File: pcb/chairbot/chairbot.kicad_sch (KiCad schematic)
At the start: 16 parts, among them J1 Conn_01x02, J2 Conn_01x05, J6 GND, U1 ESP32mini, U3 74HCT244, U4 buck-converter, U9 PCA9515

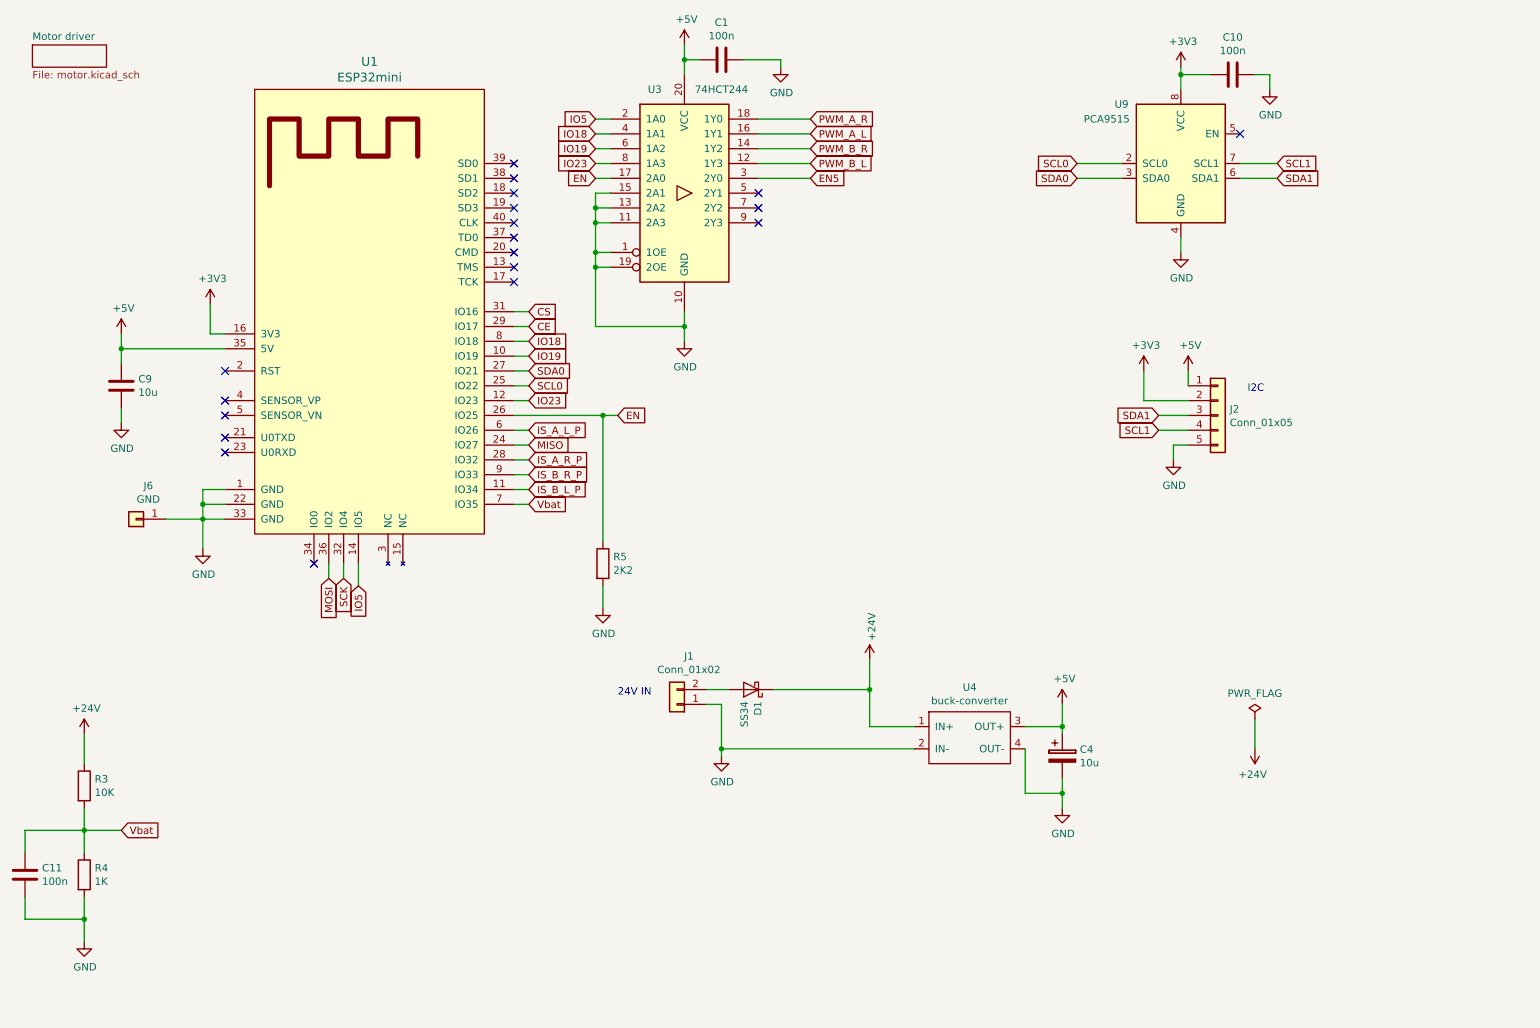
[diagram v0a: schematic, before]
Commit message: Complete overall schematic.
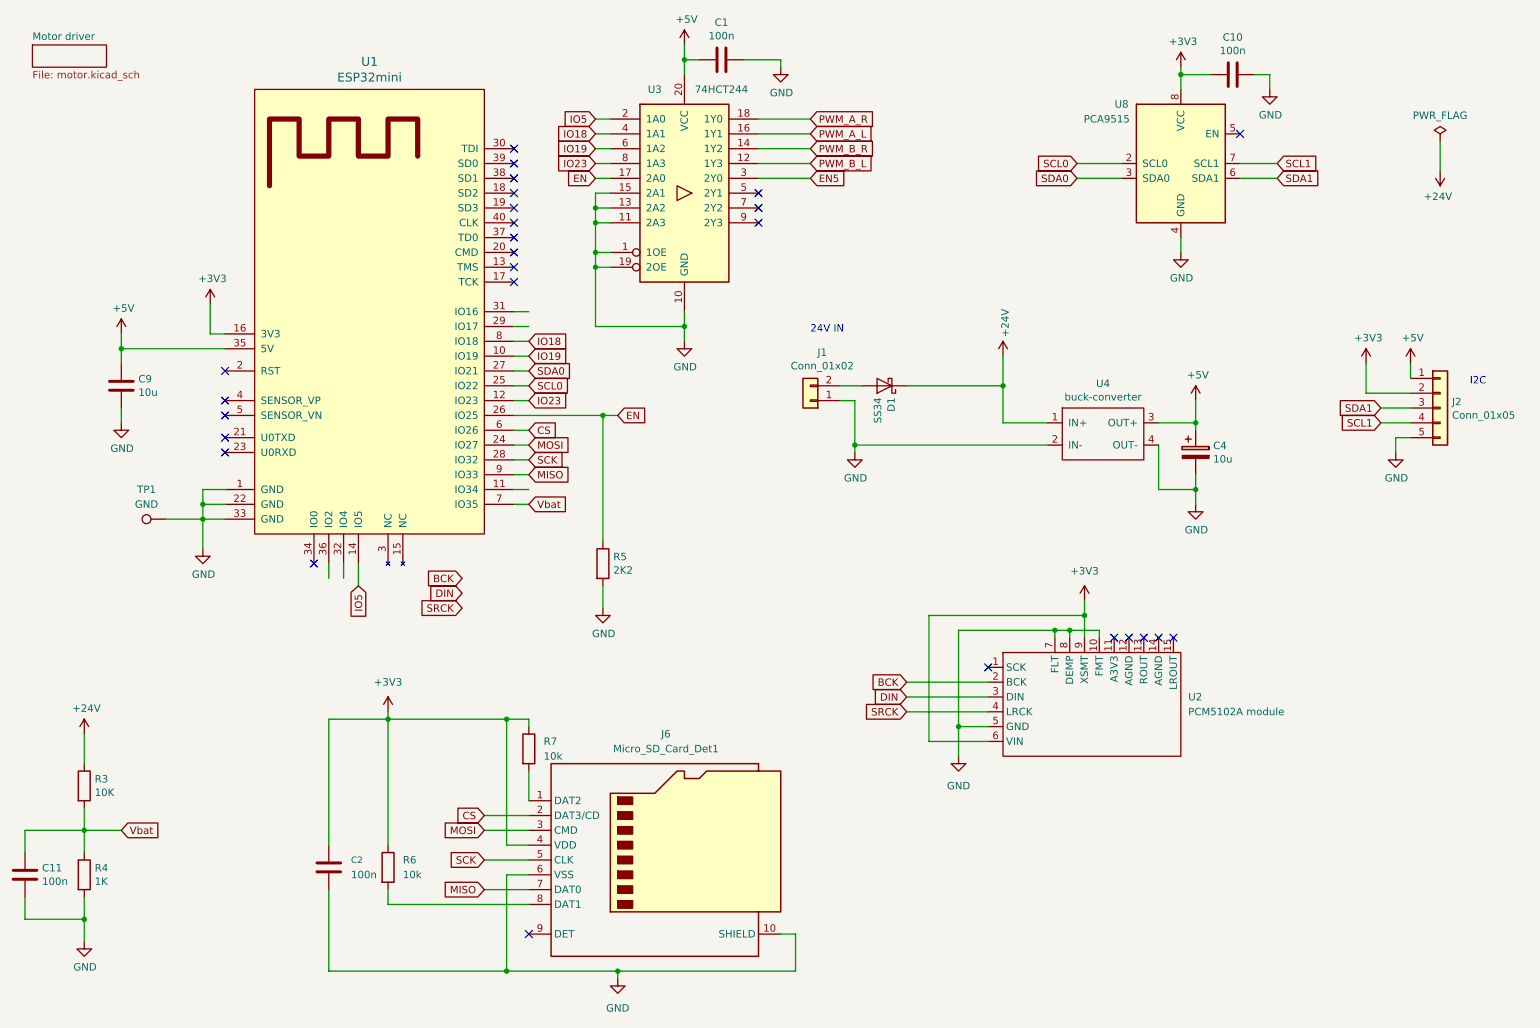
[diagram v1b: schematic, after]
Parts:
- removed J6: GND, Connector_Pin:Pin_D1.3mm_L11.0mm, symbol Connector_Generic:Conn_01x01
- added C2: 100n, Capacitor_SMD:C_0603_1608Metric, symbol kicadunlocked:C
- added J6: Micro_SD_Card_Det1, Custom:J_SD_Card-micro_dual, symbol Connector:Micro_SD_Card_Det1
- added R6, R7: 10k, Resistor_SMD:R_0603_1608Metric, symbol Device:R
- added TP1: GND, TestPoint:TestPoint_Loop_D1.80mm_Drill1.0mm_Beaded, symbol Connector:TestPoint
- added U2: PCM5102A module, Custom:PCM5102A module, symbol Custom:PCM51XX_Module
- renumbered U9 to U8
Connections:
- net IS_A_L_P is gone; now on net CS: U1.6 (IO26)
- net IS_A_R_P is gone; now on net SCK: U1.28 (IO32)
- net IS_B_R_P is gone; now on net MISO: U1.9 (IO33)
- net +3V3: now also C2.1, J6.4 (VDD), R6.1, R7.1, U2.6 (VIN), U2.9 (XSMT)
- net CS: now also J6.2 (DAT3/CD); no longer U1.31 (IO16)
- net GND: now also C2.2, J6.10 (SHIELD), J6.6 (VSS), TP1.1, U2.10 (FMT), U2.5 (GND), U2.7 (FLT), U2.8 (DEMP)
- net MISO: now also J6.7 (DAT0); no longer U1.24 (IO27)
- net MOSI: now also U1.24 (IO27), J6.3 (CMD); no longer U1.36 (IO2)
- net SCK: now also J6.5 (CLK); no longer U1.32 (IO4)
- net CE: no longer names the net of U1.29 (IO17)
- net IS_B_L_P: no longer names the net of U1.11 (IO34)
- new net: J6.8 (DAT1), R6.2
- new net: J6.1 (DAT2), R7.2
- new net BCK: U2.2 (BCK)
- new net DIN: U2.3 (DIN)
- new net SRCK: U2.4 (LRCK)
- no-connect marks 19 -> 27
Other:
- moved on the sheet: C4, D1, J1, J2, U4

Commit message: Fix errors.
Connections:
- net CS: now also U1.32 (IO4); no longer U1.6 (IO26)
- net MISO: now also U1.29 (IO17); no longer U1.9 (IO33)
- net MOSI: now also U1.31 (IO16); no longer U1.24 (IO27)
- no-connect marks 27 -> 28
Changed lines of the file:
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@@
+	)
+	(no_connect
+		(at 73.66 111.76)
 	)
 	(no_connect
@@
 	(wire
 		(pts
-			(xy 73.66 111.76) (xy 73.66 114.3)
-		)
-		(stroke
-			(width 0)
-			(type default)
-		)
-	)
-	(wire
-		(pts
 			(xy 76.2 111.76) (xy 76.2 114.3)
 		)
@@
 	(global_label "MOSI"
 		(shape input)
-		(at 107.95 91.44 0)
+		(at 107.95 68.58 0)
 		(effects
 			(font
@@
 		)
 		(property "Intersheetrefs" "${INTERSHEET_REFS}"
-			(at 107.95 91.44 0)
+			(at 107.95 68.58 0)
 			(hide yes)
 			(show_name no)
@@
 	(global_label "CS"
 		(shape input)
-		(at 107.95 88.9 0)
+		(at 76.2 114.3 270)
 		(fields_autoplaced yes)
 		(effects
@@
 				(size 1.27 1.27)
 			)
-			(justify left)
-		)
-		(property "Intersheetrefs" "${INTERSHEET_REFS}"
-			(at 112.7605 88.9 0)
-			(hide yes)
-			(show_name no)
-			(do_not_autoplace no)
-			(effects
-				(font
-					(size 1.27 1.27)
-				)
-				(justify left)
+			(justify right)
+		)
+		(property "Intersheetrefs" "${INTERSHEET_REFS}"
+			(at 76.2 119.1105 90)
+			(hide yes)
+			(show_name no)
+			(do_not_autoplace no)
+			(effects
+				(font
+					(size 1.27 1.27)
+				)
+				(justify right)
 			)
 		)
@@
 	(global_label "MISO"
 		(shape input)
-		(at 107.95 96.52 0)
+		(at 107.95 71.12 0)
 		(effects
 			(font
@@
 		)
 		(property "Intersheetrefs" "${INTERSHEET_REFS}"
-			(at 107.95 96.52 0)
-			(hide yes)
-			(show_name no)
+			(at 107.95 71.12 0)
+			(hide yes)
+			(show_name no)

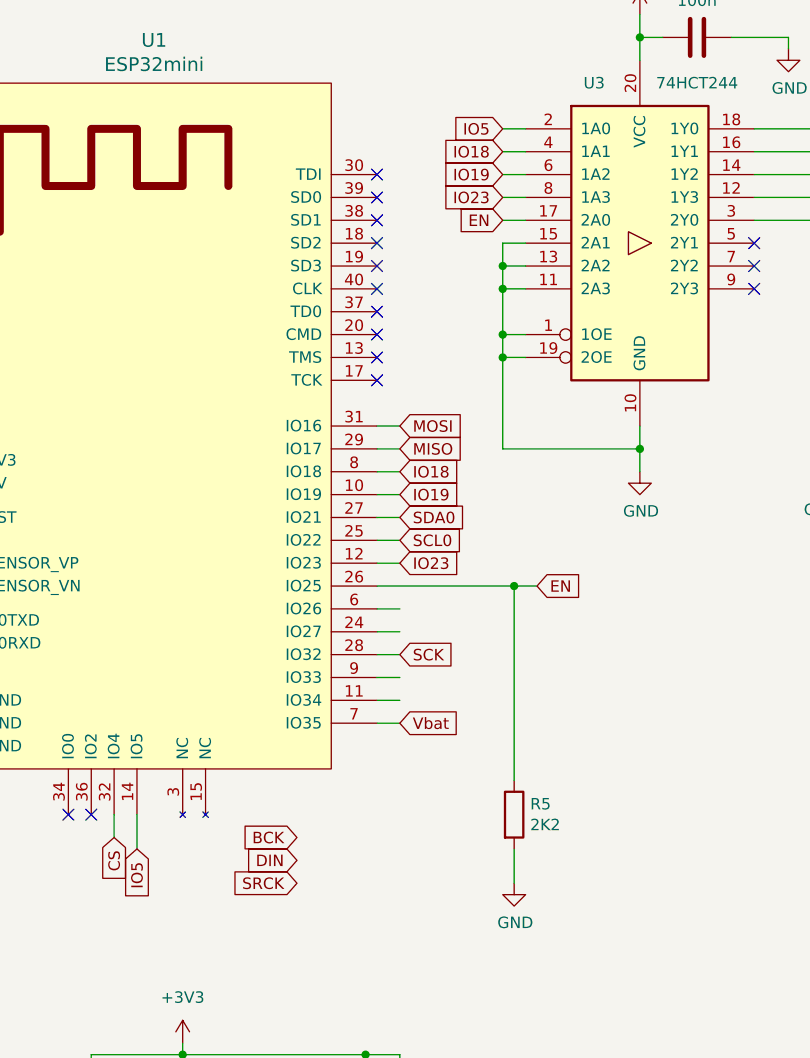
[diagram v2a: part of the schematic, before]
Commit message: Complete routing.
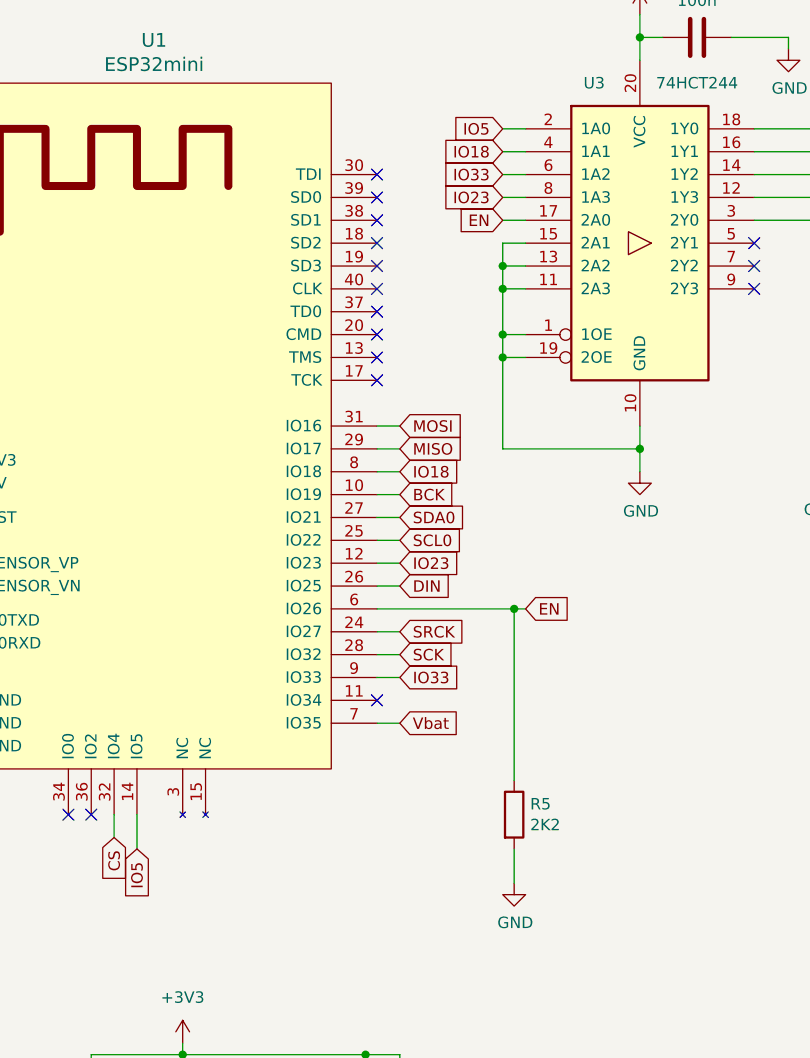
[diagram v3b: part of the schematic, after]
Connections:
- net BCK: now also U1.10 (IO19)
- net DIN: now also U1.26 (IO25)
- net EN: now also U1.6 (IO26); no longer U1.26 (IO25)
- net SRCK: now also U1.24 (IO27)
- net IO33: now reaches U1.9 (IO33)
- net IO33: now also U3.6 (1A2)
- removed net IO19: U1.10 (IO19), U3.6 (1A2)
- no-connect marks 28 -> 29
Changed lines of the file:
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@@
-	)
-	(junction
-		(at 120.65 86.36)
-		(diameter 0)
-		(color 0 0 0 0)
 	)
 	(junction
@@
 	)
 	(junction
+		(at 120.65 88.9)
+		(diameter 0)
+		(color 0 0 0 0)
+	)
+	(junction
 		(at 31.75 172.72)
 		(diameter 0)
@@
 	)
 	(no_connect
+		(at 105.41 99.06)
+	)
+	(no_connect
 		(at 105.41 53.34)
 	)
@@
 	(wire
 		(pts
-			(xy 107.95 99.06) (xy 105.41 99.06)
-		)
-		(stroke
-			(width 0)
-			(type default)
-		)
-	)
-	(wire
-		(pts
 			(xy 119.38 38.1) (xy 121.92 38.1)
 		)
@@
 	(wire
 		(pts
-			(xy 105.41 88.9) (xy 107.95 88.9)
+			(xy 105.41 88.9) (xy 120.65 88.9)
 		)
 		(stroke
@@
 	(wire
 		(pts
-			(xy 120.65 107.95) (xy 120.65 86.36)
-		)
-		(stroke
-			(width 0)
-			(type default)
-		)
-	)
-	(wire
-		(pts
 			(xy 121.92 35.56) (xy 119.38 35.56)
 		)
@@
 	(wire
 		(pts
+			(xy 120.65 88.9) (xy 120.65 107.95)
+		)
+		(stroke
+			(width 0)
+			(type default)
+		)
+	)
+	(wire
+		(pts
 			(xy 205.74 123.19) (xy 200.66 123.19)
 		)
@@
 	(wire
 		(pts
-			(xy 105.41 86.36) (xy 120.65 86.36)
-		)
-		(stroke
-			(width 0)
-			(type default)
-		)
-	)
-	(wire
-		(pts
 			(xy 153.67 181.61) (xy 123.19 181.61)
 		)
@@
 	(wire
 		(pts
+			(xy 120.65 88.9) (xy 121.92 88.9)
+		)
+		(stroke
+			(width 0)
+			(type default)
+		)
+	)
+	(wire
+		(pts
 			(xy 100.33 157.48) (xy 107.95 157.48)
 		)
@@
 	(wire
 		(pts
-			(xy 120.65 86.36) (xy 123.19 86.36)
-		)
-		(stroke
-			(width 0)
-			(type default)
-		)
-	)
-	(wire
-		(pts
 			(xy 134.62 25.4) (xy 137.16 25.4)
 		)
@@
 	(wire
 		(pts
+			(xy 105.41 86.36) (xy 107.95 86.36)
+		)
+		(stroke
+			(width 0)
+			(type default)
+		)
+	)
+	(wire
+		(pts
 			(xy 147.32 40.64) (xy 156.21 40.64)
 		)
@@
 		)
 	)
-	(global_label "IO19"
+	(global_label "IO33"
 		(shape input)
 		(at 119.38 40.64 180)
@@
 	(global_label "DIN"
 		(shape input)
-		(at 96.52 116.84 180)
+		(at 107.95 86.36 0)
 		(fields_autoplaced yes)
 		(effects
@@
 				(size 1.27 1.27)
 			)
-			(justify right)
-		)
-		(property "Intersheetrefs" "${INTERSHEET_REFS}"
-			(at 90.9837 116.84 0)
-			(hide yes)
-			(show_name no)
-			(do_not_autoplace no)
-			(effects
-				(font
-					(size 1.27 1.27)
-				)
-				(justify right)
+			(justify left)
+		)
+		(property "Intersheetrefs" "${INTERSHEET_REFS}"
+			(at 113.4863 86.36 0)
+			(hide yes)
+			(show_name no)
+			(do_not_autoplace no)
+			(effects
+				(font
+					(size 1.27 1.27)
+				)
+				(justify left)
 			)
 		)
@@
 	(global_label "SRCK"
 		(shape input)
-		(at 96.52 119.38 180)
+		(at 107.95 91.44 0)
 		(fields_autoplaced yes)
 		(effects
@@
 				(size 1.27 1.27)
 			)
-			(justify right)
-		)
-		(property "Intersheetrefs" "${INTERSHEET_REFS}"
-			(at 89.1695 119.38 0)
-			(hide yes)
-			(show_name no)
-			(do_not_autoplace no)
-			(effects
-				(font
-					(size 1.27 1.27)
-				)
-				(justify right)
-			)
-		)
-	)
-	(global_label "IO19"
-		(shape input)
-		(at 107.95 76.2 0)
-		(effects
-			(font
-				(size 1.27 1.27)
-			)
 			(justify left)
 		)
 		(property "Intersheetrefs" "${INTERSHEET_REFS}"
-			(at 107.95 76.2 0)
+			(at 115.3005 91.44 0)
+			(hide yes)
+			(show_name no)
+			(do_not_autoplace no)
+			(effects
+				(font
+					(size 1.27 1.27)
+				)
+				(justify left)
+			)
+		)
+	)
+	(global_label "IO33"
+		(shape input)
+		(at 107.95 96.52 0)
+		(effects
+			(font
+				(size 1.27 1.27)
+			)
+			(justify left)
+		)
+		(property "Intersheetrefs" "${INTERSHEET_REFS}"
+			(at 107.95 96.52 0)
 			(hide yes)
 			(show_name no)
@@
 	(global_label "BCK"
 		(shape input)
-		(at 96.52 114.3 180)
+		(at 107.95 76.2 0)
 		(fields_autoplaced yes)
 		(effects
@@
 				(size 1.27 1.27)
 			)
+			(justify left)
+		)
+		(property "Intersheetrefs" "${INTERSHEET_REFS}"
+			(at 114.091 76.2 0)
+			(hide yes)
+			(show_name no)
+			(do_not_autoplace no)
+			(effects
+				(font
+					(size 1.27 1.27)
+				)
+				(justify left)
+			)
+		)
+	)
+	(global_label "Vbat"
+		(shape input)
+		(at 38.1 157.48 0)
+		(effects
+			(font
+				(size 1.27 1.27)
+			)
+			(justify left)
+		)
+		(property "Intersheetrefs" "${INTERSHEET_REFS}"
+			(at 38.1 157.48 0)
+			(hide yes)
+			(show_name no)
+			(do_not_autoplace no)
+			(effects
+				(font
+					(size 1.27 1.27)
+				)
+			)
+		)
+	)
+	(global_label "SCL1"
+		(shape input)
+		(at 254 87.63 180)
+		(effects
+			(font
+				(size 1.27 1.27)
+			)
 			(justify right)
 		)
 		(property "Intersheetrefs" "${INTERSHEET_REFS}"
-			(at 90.379 114.3 0)
-			(hide yes)
-			(show_name no)
-			(do_not_autoplace no)
-			(effects
-				(font
-					(size 1.27 1.27)
-				)
-				(justify right)
-			)
-		)
-	)
-	(global_label "Vbat"
-		(shape input)
-		(at 38.1 157.48 0)
+			(at 254 87.63 0)
+			(hide yes)
+			(show_name no)
+			(do_not_autoplace no)
+			(effects
+				(font
+					(size 1.27 1.27)
+				)
+			)
+		)
+	)
+	(global_label "EN"
+		(shape input)
+		(at 121.92 88.9 0)
 		(effects
 			(font
@@
 		)
 		(property "Intersheetrefs" "${INTERSHEET_REFS}"
-			(at 38.1 157.48 0)
-			(hide yes)
-			(show_name no)
-			(do_not_autoplace no)
-			(effects
-				(font
-					(size 1.27 1.27)
-				)
-			)
-		)
-	)
-	(global_label "SCL1"
-		(shape input)
-		(at 254 87.63 180)
-		(effects
-			(font
-				(size 1.27 1.27)
-			)
-			(justify right)
-		)
-		(property "Intersheetrefs" "${INTERSHEET_REFS}"
-			(at 254 87.63 0)
-			(hide yes)
-			(show_name no)
-			(do_not_autoplace no)
-			(effects
-				(font
-					(size 1.27 1.27)
-				)
-			)
-		)
-	)
-	(global_label "EN"
-		(shape input)
-		(at 123.19 86.36 0)
-		(effects
-			(font
-				(size 1.27 1.27)
-			)
-			(justify left)
-		)
-		(property "Intersheetrefs" "${INTERSHEET_REFS}"
-			(at 123.19 86.36 0)
-			(hide yes)
-			(show_name no)
+			(at 121.92 88.9 0)
+			(hide yes)
+			(show_name no)
